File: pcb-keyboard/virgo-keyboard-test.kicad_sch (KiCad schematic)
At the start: 242 parts, among them J1 Conn_ARM_SWD_TagConnect_TC2030, J2 AFC07-S20FCC-00, J3 F1004-H-08-20G-R, J4 F1004-H-08-20G-R, SW1 SKRPACE010, SW2 SKRPACE010, SW3 SKRPACE010, U4 W25Q16JVSSIQ, U5 RP2040, Y1 RH100-12.000-18-2030-TR

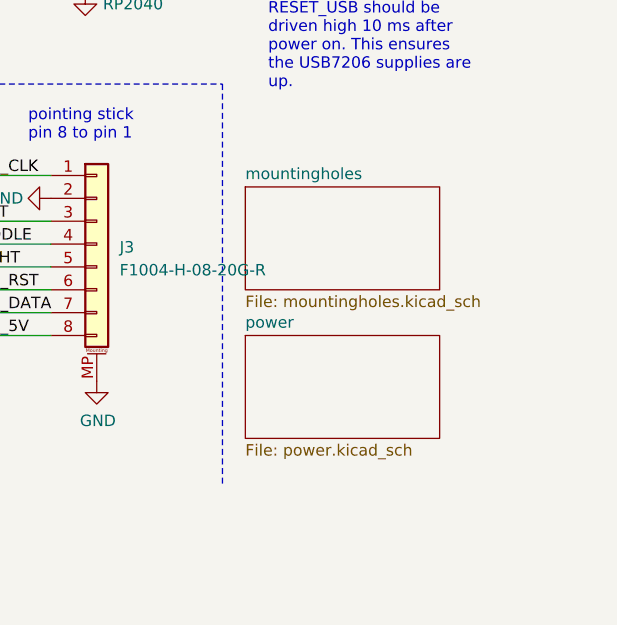
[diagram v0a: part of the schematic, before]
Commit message: Spacing changes to virgo keyboard
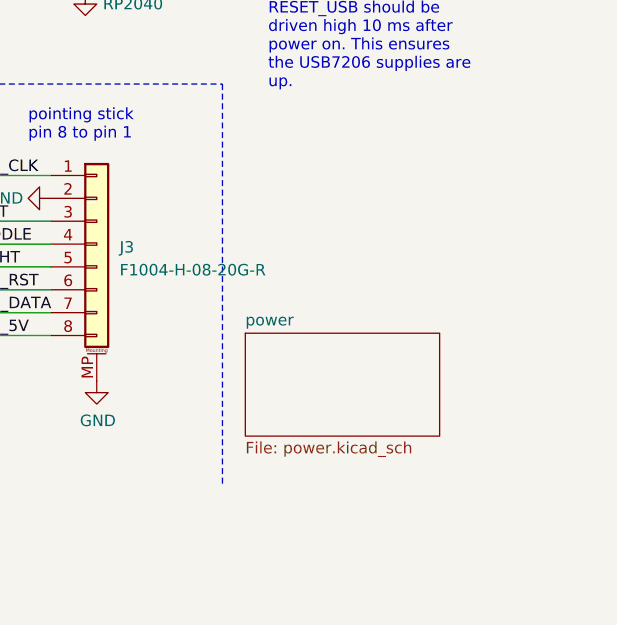
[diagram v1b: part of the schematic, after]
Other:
- removed sheet mountingholes
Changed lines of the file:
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@@
     )
   )
-  (sheet (at 377.19 219.71) (size 21.59 11.43) (fields_autoplaced)
-    (stroke (width 0.1524) (type solid))
+  (sheet (at 377.19 235.966) (size 21.59 11.43) (fields_autoplaced)
+    (stroke (width 0) (type solid))
     (fill (color 0 0 0 0.0000))
-    (property "Sheetname" "mountingholes" (at 377.19 218.9984 0)
+    (property "Sheetname" "power" (at 377.19 235.2544 0)
       (effects (font (size 1.27 1.27)) (justify left bottom))
     )
-    (property "Sheetfile" "mountingholes.kicad_sch" (at 377.19 231.7246 0)
+    (property "Sheetfile" "power.kicad_sch" (at 377.19 247.9806 0)
       (effects (font (size 1.27 1.27)) (justify left top))
     )
-    (instances
-      (project "virgo-keyboard-test"
-        (path "/80c969df-cd39-4c4a-8336-5a366308cfd3" (page "3"))
-      )
-    )
-  )
-  (sheet (at 377.19 236.22) (size 21.59 11.43) (fields_autoplaced)
-    (stroke (width 0) (type solid))
-    (fill (color 0 0 0 0.0000))
-    (property "Sheetname" "power" (at 377.19 235.5084 0)
-      (effects (font (size 1.27 1.27)) (justify left bottom))
-    )
-    (property "Sheetfile" "power.kicad_sch" (at 377.19 248.2346 0)
-      (effects (font (size 1.27 1.27)) (justify left top))
-    )
